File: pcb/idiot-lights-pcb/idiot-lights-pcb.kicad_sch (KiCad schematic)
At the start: 71 parts, among them Q1 BSS138, Q10 BSS138, Q11 BSS138, Q12 BSS138, Q13 BSS138, Q14 BSS138, Q15 BSS138, Q16 BSS138, Q2 BSS138, Q3 BSS138, Q4 BSS138, Q5 BSS138, Q6 BSS138, Q7 BSS138, Q8 BSS138, Q9 BSS138, SW1 Toggle left indicator, SW2 Toggle right indicator, SW3 Toggle hazard warning, SW4 Break control, SW5 Reset, U1 RaspberryPi_Pico

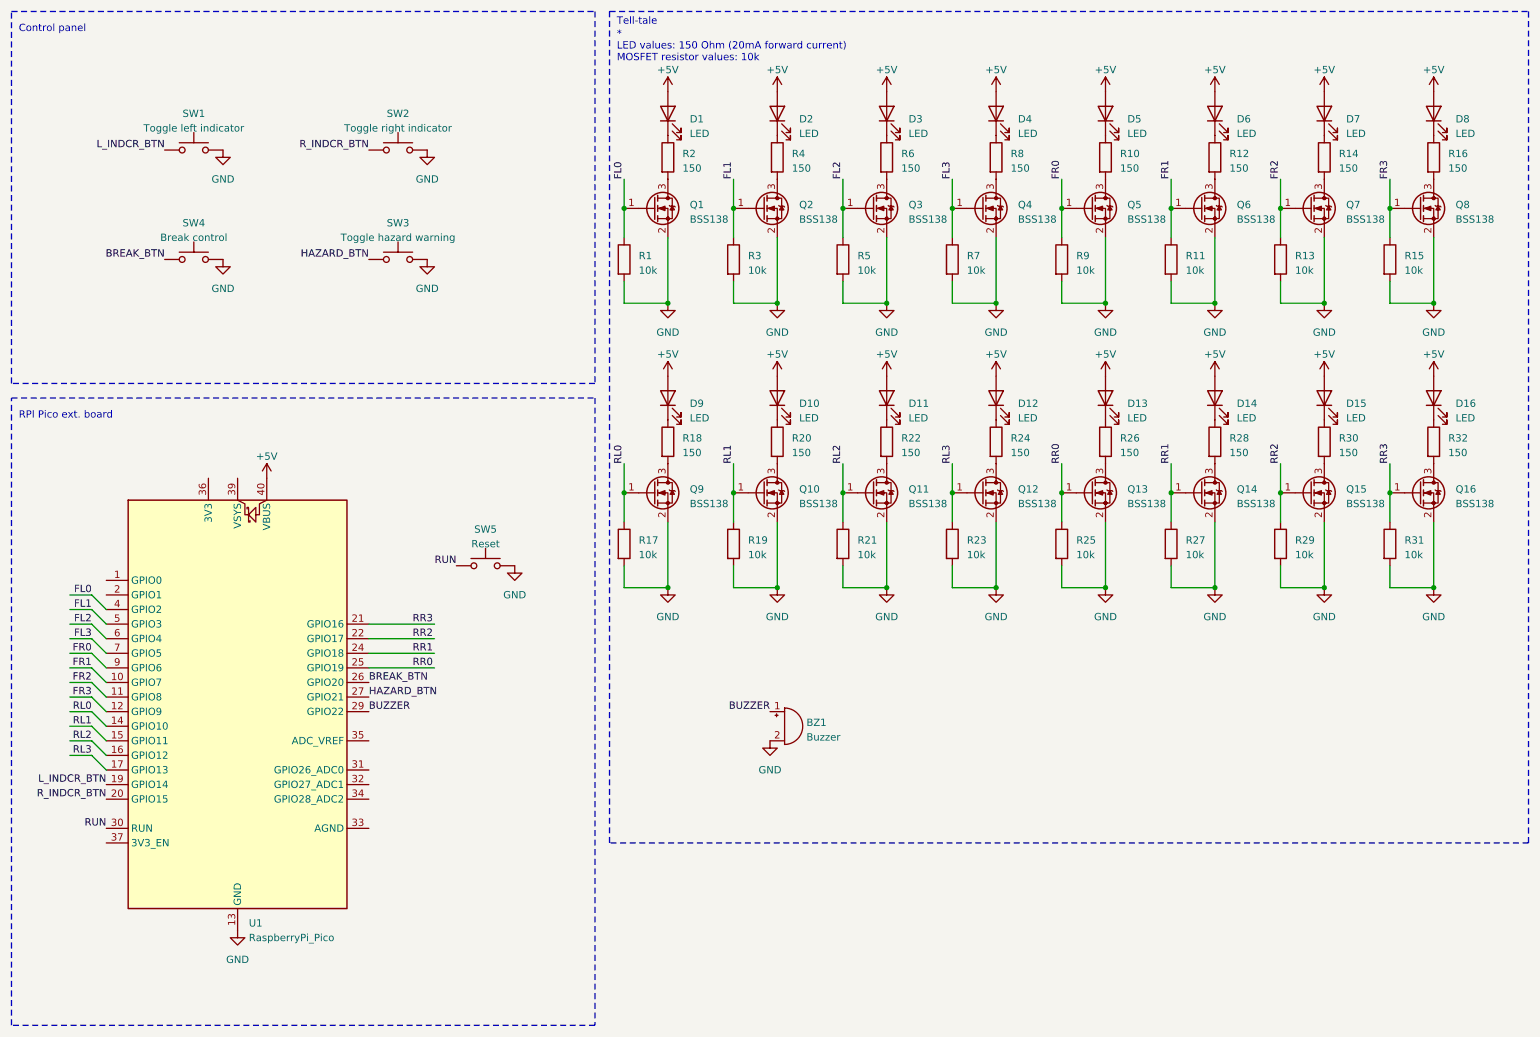
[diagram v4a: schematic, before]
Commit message: Add gate resistors and re-reoute symbols
Bump version text to v.1.2
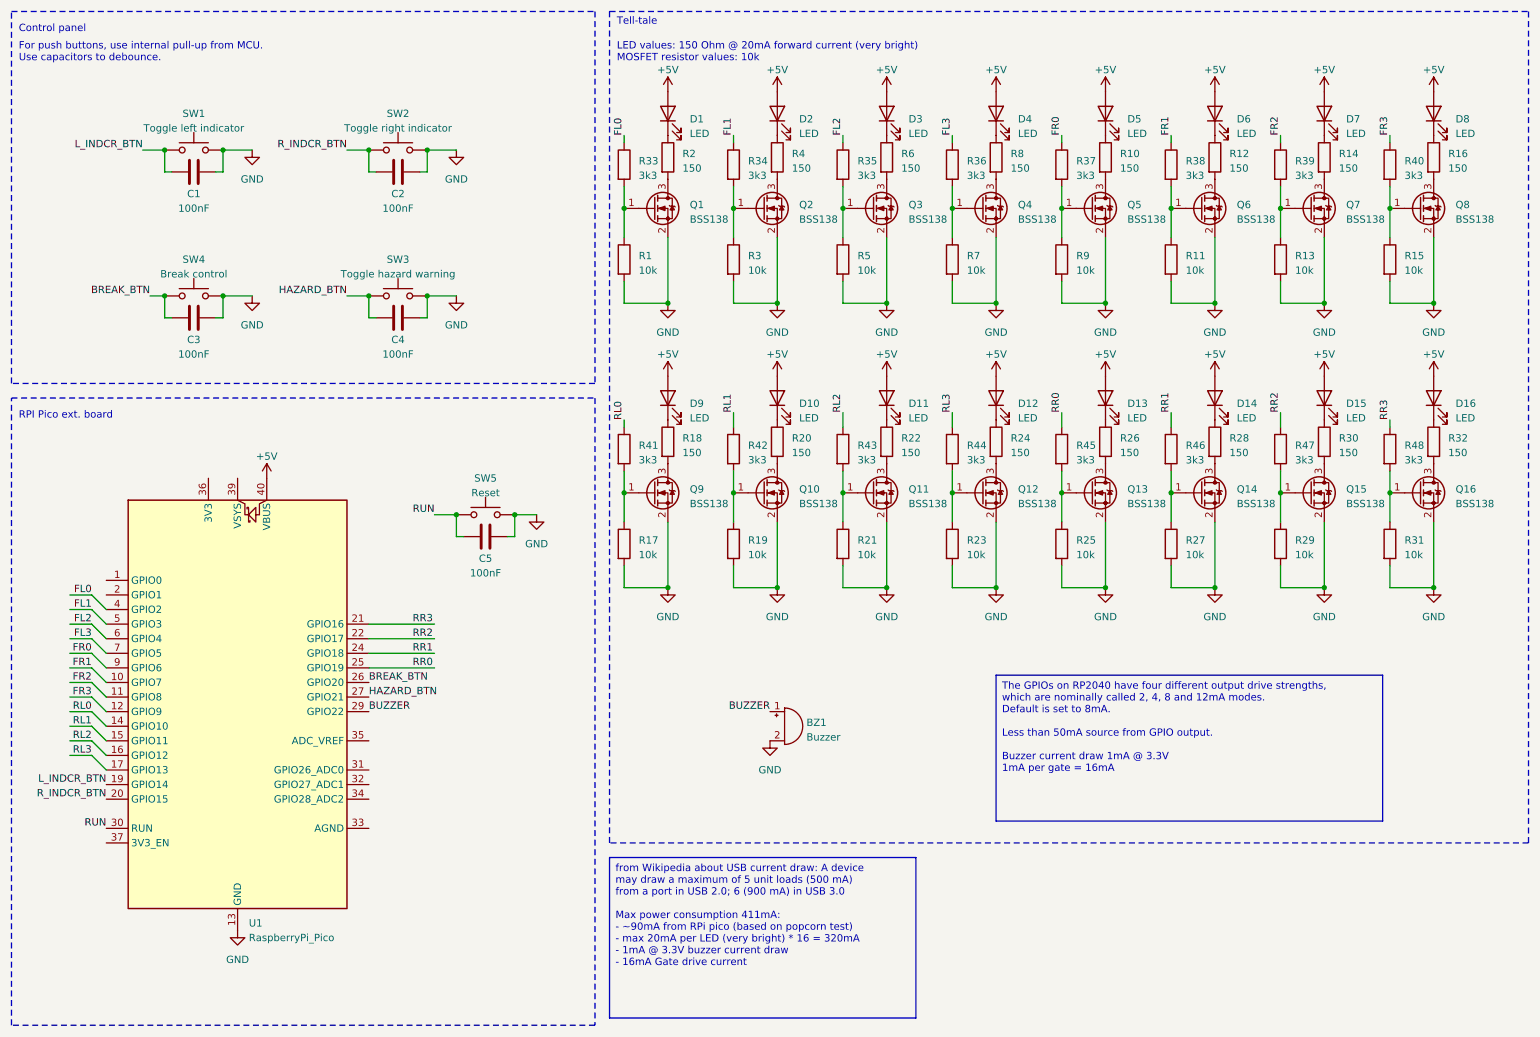
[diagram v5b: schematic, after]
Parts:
- added C1, C2, C3, C4, C5: 100nF, Capacitor_SMD:C_0603_1608Metric, symbol Device:C
- added R33, R34, R35, R36, R37, R38, R39, R40, R41, R42, R43, R44, R45, R46, R47, R48: 3k3, Resistor_SMD_no_silk:R_0603_1608Metric_no_silk, symbol Device:R
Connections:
- net BREAK_BTN: now also C3.1
- net FL0: now also R33.1; no longer Q1.1 (G), R1.1
- net FL1: now also R34.1; no longer Q2.1 (G), R3.1
- net FL2: now also R35.1; no longer Q3.1 (G), R5.1
- net FL3: now also R36.1; no longer Q4.1 (G), R7.1
- net FR0: now also R37.1; no longer Q5.1 (G), R9.1
- net FR1: now also R38.1; no longer Q6.1 (G), R11.1
- net FR2: now also R39.1; no longer Q7.1 (G), R13.1
- net FR3: now also R40.1; no longer Q8.1 (G), R15.1
- net GND: now also C1.2, C2.2, C3.2, C4.2, C5.2
- net HAZARD_BTN: now also C4.1
- net L_INDCR_BTN: now also C1.1
- net RL0: now also R41.1; no longer Q9.1 (G), R17.1
- net RL1: now also R42.1; no longer Q10.1 (G), R19.1
- net RL2: now also R43.1; no longer Q11.1 (G), R21.1
- net RL3: now also R44.1; no longer Q12.1 (G), R23.1
- net RR0: now also R45.1; no longer Q13.1 (G), R25.1
- net RR1: now also R46.1; no longer Q14.1 (G), R27.1
- net RR2: now also R47.1; no longer Q15.1 (G), R29.1
- net RR3: now also R48.1; no longer Q16.1 (G), R31.1
- net RUN: now also C5.1
- net R_INDCR_BTN: now also C2.1
- new net: Q3.1 (G), R35.2, R5.1
- new net: Q13.1 (G), R25.1, R45.2
- new net: Q15.1 (G), R29.1, R47.2
- new net: Q2.1 (G), R3.1, R34.2
- new net: Q7.1 (G), R13.1, R39.2
- new net: Q1.1 (G), R1.1, R33.2
- new net: Q10.1 (G), R19.1, R42.2
- new net: Q5.1 (G), R37.2, R9.1
- new net: Q16.1 (G), R31.1, R48.2
- new net: Q9.1 (G), R17.1, R41.2
- new net: Q4.1 (G), R36.2, R7.1
- new net: Q11.1 (G), R21.1, R43.2
- new net: Q12.1 (G), R23.1, R44.2
- new net: Q14.1 (G), R27.1, R46.2
- new net: Q8.1 (G), R15.1, R40.2
- new net: Q6.1 (G), R11.1, R38.2
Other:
- note added: "For push buttons, use internal pull-up from MCU. Use capacitors to debounce."
- note added: "LED values: 150 Ohm @ 20mA forward current (very bright) MOSFET resistor values: 10k"
- note removed: "* LED values: 150 Ohm (20mA forward current) MOSFET resistor values: 10k"
- moved on the sheet: SW3, SW4, SW5

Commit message: Fix resistor values
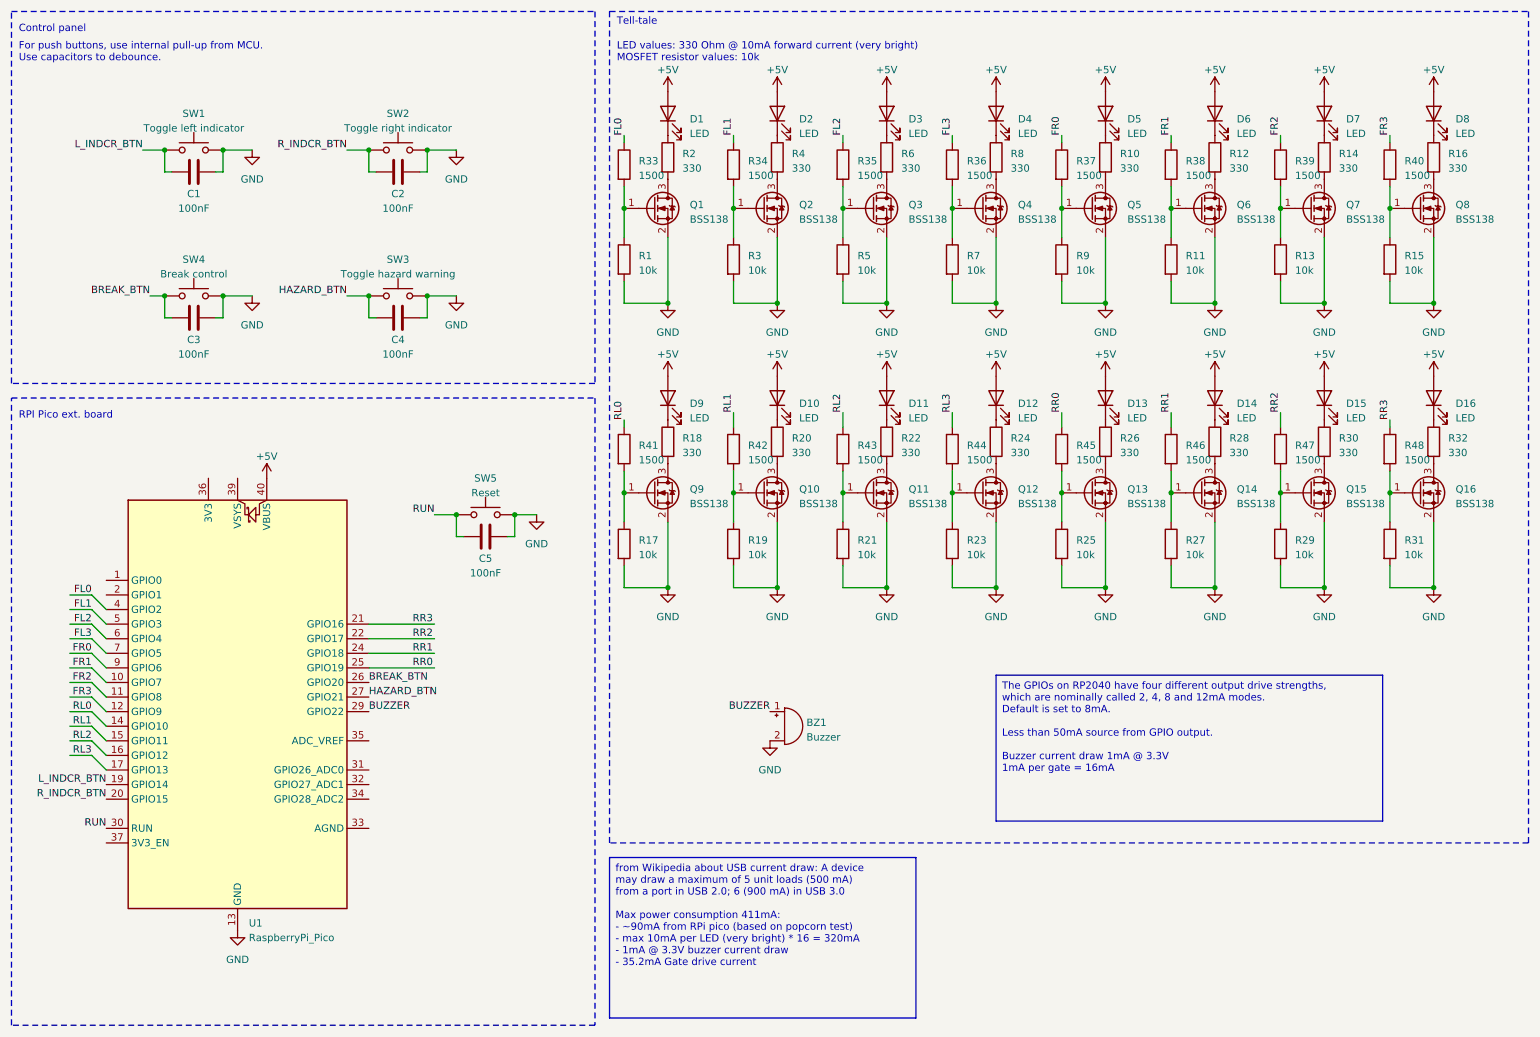
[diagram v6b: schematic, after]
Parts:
- R10, R12, R14, R16, R18, R2, R20, R22, R24, R26, R28, R30, R32, R4, R6, R8: value 150 -> 330
- R33, R34, R35, R36, R37, R38, R39, R40, R41, R42, R43, R44, R45, R46, R47, R48: value 3k3 -> 1500
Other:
- note added: "LED values: 330 Ohm @ 10mA forward current (very bright) MOSFET resistor values: 10k"
- note removed: "LED values: 150 Ohm @ 20mA forward current (very bright) MOSFET resistor values: 10k"
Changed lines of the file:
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@@
     (effects (font (size 1.27 1.27)) (justify left top))
   )
-  (text_box "from Wikipedia about USB current draw: A device may draw a maximum of 5 unit loads (500 mA) from a port in USB 2.0; 6 (900 mA) in USB 3.0\n\nMax power consumption 411mA:\n- ~90mA from RPi pico (based on popcorn test)\n- max 20mA per LED (very bright) * 16 = 320mA\n- 1mA @ 3.3V buzzer current draw\n- 16mA Gate drive current\n"
+  (text_box "from Wikipedia about USB current draw: A device may draw a maximum of 5 unit loads (500 mA) from a port in USB 2.0; 6 (900 mA) in USB 3.0\n\nMax power consumption 411mA:\n- ~90mA from RPi pico (based on popcorn test)\n- max 10mA per LED (very bright) * 16 = 320mA\n- 1mA @ 3.3V buzzer current draw\n- 35.2mA Gate drive current\n"
     (at 120.65 165.1 0) (size 53.34 27.94)
     (stroke (width 0) (type default))
@@
     (effects (font (size 1.27 1.27)) (justify left bottom))
   )
-  (text "LED values: 150 Ohm @ 20mA forward current (very bright)\nMOSFET resistor values: 10k"
+  (text "LED values: 330 Ohm @ 10mA forward current (very bright)\nMOSFET resistor values: 10k"
     (at 121.92 26.67 0)
     (effects (font (size 1.27 1.27)) (justify left bottom))
@@
       (effects (font (size 1.27 1.27)) (justify left))
     )
-    (property "Value" "3k3" (at 240.03 46.355 0)
+    (property "Value" "1500" (at 240.03 46.355 0)
       (effects (font (size 1.27 1.27)) (justify left))
     )
@@
       (effects (font (size 1.27 1.27)) (justify left))
     )
-    (property "Value" "3k3" (at 144.78 46.355 0)
+    (property "Value" "1500" (at 144.78 46.355 0)
       (effects (font (size 1.27 1.27)) (justify left))
     )
@@
       (effects (font (size 1.27 1.27)) (justify left))
     )
-    (property "Value" "150" (at 209.55 94.615 0)
+    (property "Value" "330" (at 209.55 94.615 0)
       (effects (font (size 1.27 1.27)) (justify left))
     )
@@
       (effects (font (size 1.27 1.27)) (justify left))
     )
-    (property "Value" "150" (at 133.35 94.615 0)
+    (property "Value" "330" (at 133.35 94.615 0)
       (effects (font (size 1.27 1.27)) (justify left))
     )
@@
       (effects (font (size 1.27 1.27)) (justify left))
     )
-    (property "Value" "150" (at 171.45 94.615 0)
+    (property "Value" "330" (at 171.45 94.615 0)
       (effects (font (size 1.27 1.27)) (justify left))
     )
@@
       (effects (font (size 1.27 1.27)) (justify left))
     )
-    (property "Value" "150" (at 171.45 45.085 0)
+    (property "Value" "330" (at 171.45 45.085 0)
       (effects (font (size 1.27 1.27)) (justify left))
     )
@@
       (effects (font (size 1.27 1.27)) (justify left))
     )
-    (property "Value" "3k3" (at 182.88 46.355 0)
+    (property "Value" "1500" (at 182.88 46.355 0)
       (effects (font (size 1.27 1.27)) (justify left))
     )
@@
       (effects (font (size 1.27 1.27)) (justify left))
     )
-    (property "Value" "150" (at 228.6 94.615 0)
+    (property "Value" "330" (at 228.6 94.615 0)
       (effects (font (size 1.27 1.27)) (justify left))
     )
@@
       (effects (font (size 1.27 1.27)) (justify left))
     )
-    (property "Value" "150" (at 247.65 45.085 0)
+    (property "Value" "330" (at 247.65 45.085 0)
       (effects (font (size 1.27 1.27)) (justify left))
     )
@@
       (effects (font (size 1.27 1.27)) (justify left))
     )
-    (property "Value" "150" (at 133.35 45.085 0)
+    (property "Value" "330" (at 133.35 45.085 0)
       (effects (font (size 1.27 1.27)) (justify left))
     )
@@
       (effects (font (size 1.27 1.27)) (justify left))
     )
-    (property "Value" "3k3" (at 144.78 95.885 0)
+    (property "Value" "1500" (at 144.78 95.885 0)
       (effects (font (size 1.27 1.27)) (justify left))
     )
@@
       (effects (font (size 1.27 1.27)) (justify left))
     )
-    (property "Value" "150" (at 209.55 45.085 0)
+    (property "Value" "330" (at 209.55 45.085 0)
       (effects (font (size 1.27 1.27)) (justify left))
     )
@@
       (effects (font (size 1.27 1.27)) (justify left))
     )
-    (property "Value" "150" (at 152.4 94.615 0)
+    (property "Value" "330" (at 152.4 94.615 0)
       (effects (font (size 1.27 1.27)) (justify left))
     )
@@
       (effects (font (size 1.27 1.27)) (justify left))
     )
-    (property "Value" "3k3" (at 125.73 95.885 0)
+    (property "Value" "1500" (at 125.73 95.885 0)
       (effects (font (size 1.27 1.27)) (justify left))
     )
@@
       (effects (font (size 1.27 1.27)) (justify left))
     )
-    (property "Value" "3k3" (at 240.03 95.885 0)
+    (property "Value" "1500" (at 240.03 95.885 0)
       (effects (font (size 1.27 1.27)) (justify left))
     )
@@
       (effects (font (size 1.27 1.27)) (justify left))
     )
-    (property "Value" "3k3" (at 220.98 95.885 0)
+    (property "Value" "1500" (at 220.98 95.885 0)
       (effects (font (size 1.27 1.27)) (justify left))
     )
@@
       (effects (font (size 1.27 1.27)) (justify left))
     )
-    (property "Value" "3k3" (at 259.08 95.885 0)
+    (property "Value" "1500" (at 259.08 95.885 0)
       (effects (font (size 1.27 1.27)) (justify left))
     )
@@
       (effects (font (size 1.27 1.27)) (justify left))
     )
-    (property "Value" "150" (at 266.7 94.615 0)
+    (property "Value" "330" (at 266.7 94.615 0)
       (effects (font (size 1.27 1.27)) (justify left))
     )
@@
       (effects (font (size 1.27 1.27)) (justify left))
     )
-    (property "Value" "3k3" (at 201.93 95.885 0)
+    (property "Value" "1500" (at 201.93 95.885 0)
       (effects (font (size 1.27 1.27)) (justify left))
     )
@@
       (effects (font (size 1.27 1.27)) (justify left))
     )
-    (property "Value" "3k3" (at 259.08 46.355 0)
+    (property "Value" "1500" (at 259.08 46.355 0)
       (effects (font (size 1.27 1.27)) (justify left))
     )
@@
       (effects (font (size 1.27 1.27)) (justify left))
     )
-    (property "Value" "3k3" (at 163.83 95.885 0)
+    (property "Value" "1500" (at 163.83 95.885 0)
       (effects (font (size 1.27 1.27)) (justify left))
     )
@@
       (effects (font (size 1.27 1.27)) (justify left))
     )
-    (property "Value" "3k3" (at 220.98 46.355 0)
+    (property "Value" "1500" (at 220.98 46.355 0)
       (effects (font (size 1.27 1.27)) (justify left))
     )
@@
       (effects (font (size 1.27 1.27)) (justify left))
     )
-    (property "Value" "3k3" (at 182.88 95.885 0)
+    (property "Value" "1500" (at 182.88 95.885 0)
       (effects (font (size 1.27 1.27)) (justify left))
     )
@@
       (effects (font (size 1.27 1.27)) (justify left))
     )
-    (property "Value" "150" (at 266.7 45.085 0)
+    (property "Value" "330" (at 266.7 45.085 0)
       (effects (font (size 1.27 1.27)) (justify left))
     )
@@
       (effects (font (size 1.27 1.27)) (justify left))
     )
-    (property "Value" "3k3" (at 125.73 46.355 0)
+    (property "Value" "1500" (at 125.73 46.355 0)
       (effects (font (size 1.27 1.27)) (justify left))
     )
@@
       (effects (font (size 1.27 1.27)) (justify left))
     )
-    (property "Value" "3k3" (at 163.83 46.355 0)
+    (property "Value" "1500" (at 163.83 46.355 0)
       (effects (font (size 1.27 1.27)) (justify left))
     )
@@
       (effects (font (size 1.27 1.27)) (justify left))
     )
-    (property "Value" "150" (at 190.5 45.085 0)
+    (property "Value" "330" (at 190.5 45.085 0)
       (effects (font (size 1.27 1.27)) (justify left))
     )
@@
       (effects (font (size 1.27 1.27)) (justify left))
     )
-    (property "Value" "150" (at 152.4 45.085 0)
+    (property "Value" "330" (at 152.4 45.085 0)
       (effects (font (size 1.27 1.27)) (justify left))
     )
@@
       (effects (font (size 1.27 1.27)) (justify left))
     )
-    (property "Value" "150" (at 190.5 94.615 0)
+    (property "Value" "330" (at 190.5 94.615 0)
       (effects (font (size 1.27 1.27)) (justify left))
     )
@@
       (effects (font (size 1.27 1.27)) (justify left))
     )
-    (property "Value" "3k3" (at 201.93 46.355 0)
+    (property "Value" "1500" (at 201.93 46.355 0)
       (effects (font (size 1.27 1.27)) (justify left))
     )
@@
       (effects (font (size 1.27 1.27)) (justify left))
     )
-    (property "Value" "150" (at 247.65 94.615 0)
+    (property "Value" "330" (at 247.65 94.615 0)
       (effects (font (size 1.27 1.27)) (justify left))
     )
@@
       (effects (font (size 1.27 1.27)) (justify left))
     )
-    (property "Value" "150" (at 228.6 45.085 0)
+    (property "Value" "330" (at 228.6 45.085 0)
       (effects (font (size 1.27 1.27)) (justify left))
     )
